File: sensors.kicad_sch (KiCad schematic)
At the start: 9 parts, among them J3 Conn_01x04, U10 MPU-9250, U12 LSM6DS3

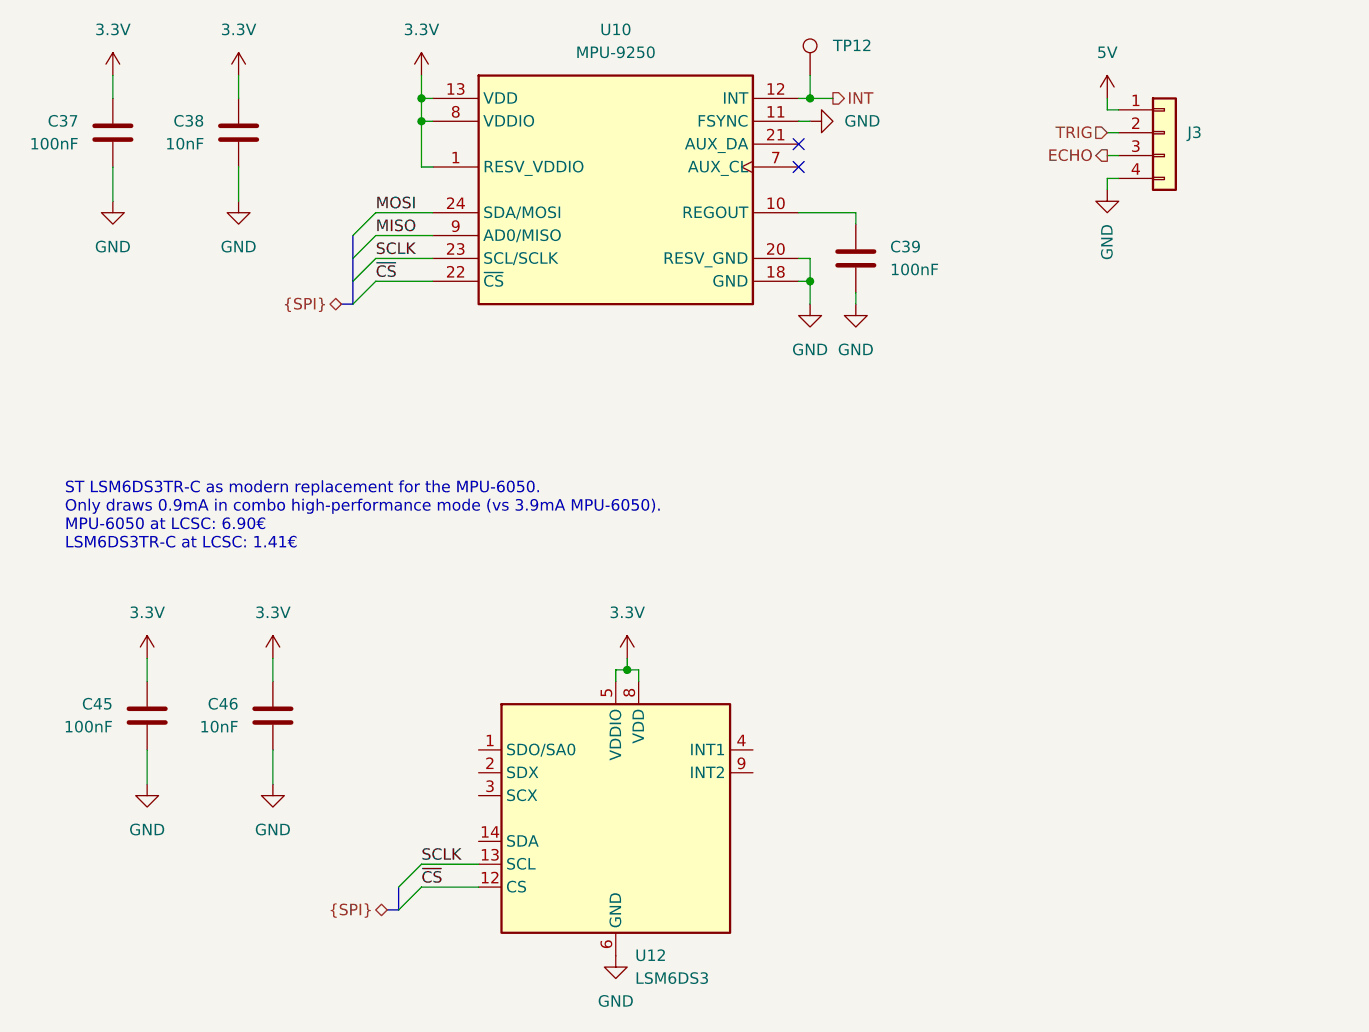
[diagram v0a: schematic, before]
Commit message: Undo component replacement
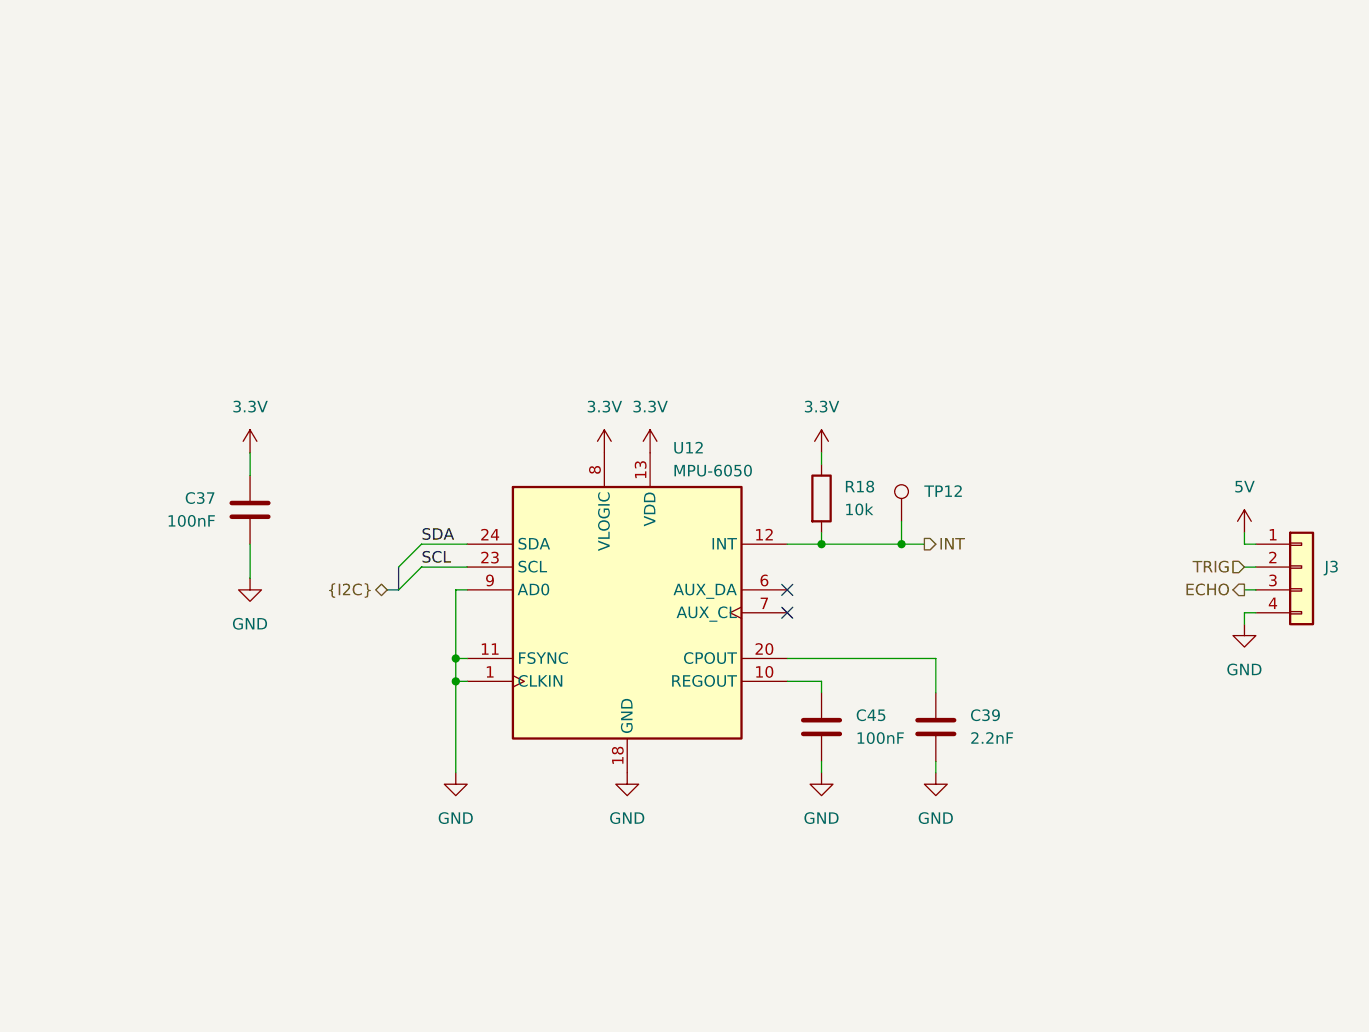
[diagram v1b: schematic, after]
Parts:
- removed C38, C46: 10nF, Capacitor_SMD:C_0402_1005Metric_Pad0.74x0.62mm_HandSolder, symbol Device:C
- removed U10: MPU-9250, Sensor_Motion:InvenSense_QFN-24_3x3mm_P0.4mm, symbol Sensor_Motion:MPU-9250
- removed U12: LSM6DS3, Package_LGA:LGA-14_3x2.5mm_P0.5mm_LayoutBorder3x4y, symbol Sensor_Motion:LSM6DS3
- added R18: 10k, symbol Device:R
- added U12: MPU-6050, Sensor_Motion:InvenSense_QFN-24_4x4mm_P0.5mm, symbol Sensor_Motion:MPU-6050
- C39: value 100nF -> 2.2nF
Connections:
- net 3.3V: now also R18.1, U12.13 (VDD), U12.8 (VLOGIC); no longer C45.1
- net GND: now also U12.1 (CLKIN), U12.11 (FSYNC), U12.18 (GND), U12.9 (AD0)
- net INT: now also R18.2, U12.12 (INT)
- net at C39.1: now also U12.20 (CPOUT)
- new net: C45.1, U12.10 (REGOUT)
- new net SCL: U12.23 (SCL)
- new net SDA: U12.24 (SDA)
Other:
- note removed: "ST LSM6DS3TR-C as modern replacement for the MPU-6050. Only draws 0.9mA in combo high-performance mode (vs 3.9mA MPU-6050). MPU-6050 at LCSC: 6.90€ LSM6DS3TR-C at LCSC: 1.41€"
- moved on the sheet: C37, C39, J3, TP12

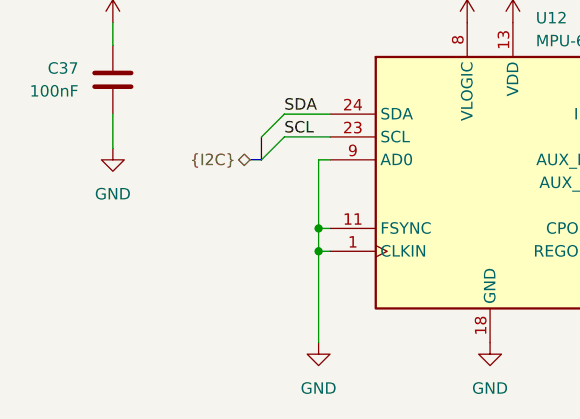
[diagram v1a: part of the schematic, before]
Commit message: Document address assignment
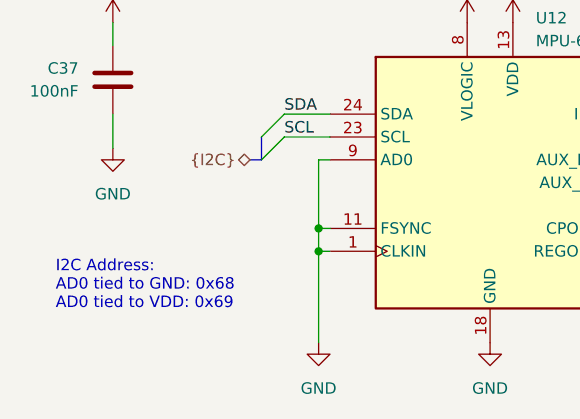
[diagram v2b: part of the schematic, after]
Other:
- note added: "I2C Address: AD0 tied to GND: 0x68 AD0 tied to VDD: 0x69"
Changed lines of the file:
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@@
 		(members "IN1" "IN2" "PWM")
+	)
+	(text "I2C Address:\nAD0 tied to GND: 0x68\nAD0 tied to VDD: 0x69"
+		(exclude_from_sim no)
+		(at 95.25 109.22 0)
+		(effects
+			(font
+				(size 1.27 1.27)
+			)
+			(justify left)
+		)
 	)
 	(junction

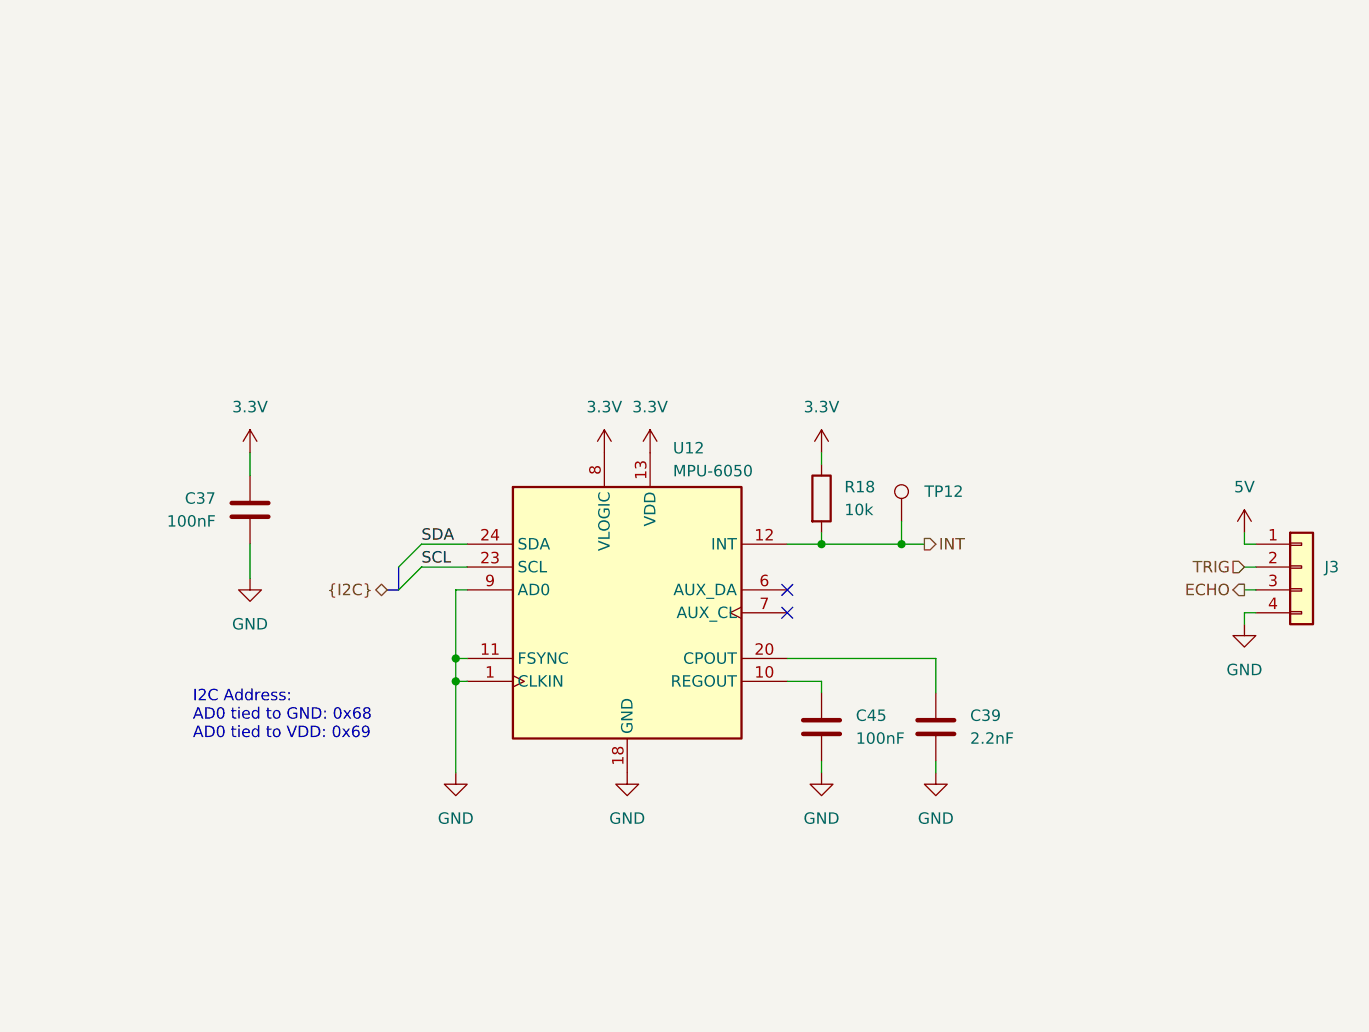
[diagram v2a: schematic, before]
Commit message: Fix sensor wiring
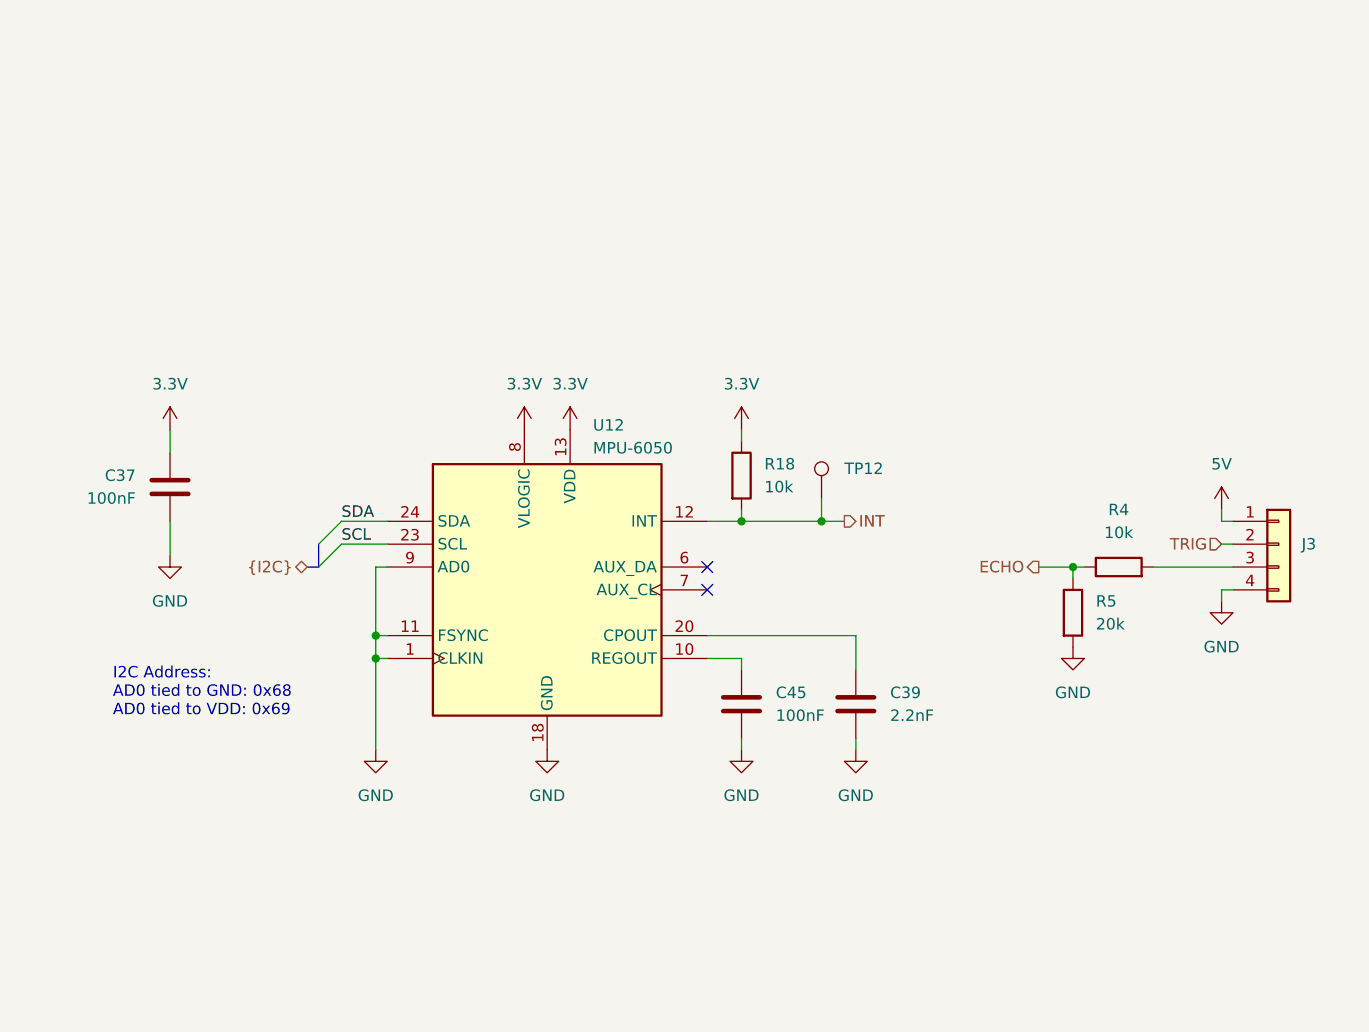
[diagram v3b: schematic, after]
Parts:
- added R4: 10k, symbol Device:R
- added R5: 20k, symbol Device:R
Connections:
- net ECHO: now also R4.1, R5.1; no longer J3.3 (Pin_3)
- net GND: now also R5.2
- new net: J3.3 (Pin_3), R4.2
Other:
- moved on the sheet: C37, C39, C45, J3, R18, TP12, U12

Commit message: Add missing pull-up for CP2102
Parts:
- renumbered C37 to C38, C45 to C39, C39 to C40, J3 to J4, R18 to R17, R4 to R18, R5 to R19, U12 to U10
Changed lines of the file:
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@@
 		(on_board yes)
 		(dnp no)
-		(property "Reference" "J3"
+		(property "Reference" "J4"
 			(at 218.44 90.1699 0)
 			(effects
@@
 			(project "Tumbler2_Redesign"
 				(path "/f3fd8d79-9d35-4c04-811e-2697a2740958/38423c09-d546-4c9c-b674-750983dc8f27"
-					(reference "J3")
+					(reference "J4")
 					(unit 1)
 				)
@@
 		(dnp no)
 		(fields_autoplaced yes)
-		(property "Reference" "#PWR0118"
+		(property "Reference" "#PWR0130"
 			(at 115.57 119.38 0)
 			(effects
@@
 			(project "Tumbler2_Redesign"
 				(path "/f3fd8d79-9d35-4c04-811e-2697a2740958/38423c09-d546-4c9c-b674-750983dc8f27"
-					(reference "#PWR0118")
+					(reference "#PWR0130")
 					(unit 1)
 				)
@@
 		(dnp no)
 		(fields_autoplaced yes)
-		(property "Reference" "#PWR0119"
+		(property "Reference" "#PWR0122"
 			(at 92.71 81.28 0)
 			(effects
@@
 			(project "Tumbler2_Redesign"
 				(path "/f3fd8d79-9d35-4c04-811e-2697a2740958/38423c09-d546-4c9c-b674-750983dc8f27"
-					(reference "#PWR0119")
+					(reference "#PWR0122")
 					(unit 1)
 				)
@@
 		(dnp no)
 		(fields_autoplaced yes)
-		(property "Reference" "#PWR0125"
+		(property "Reference" "#PWR0127"
 			(at 92.71 97.79 0)
 			(effects
@@
 			(project "Tumbler2_Redesign"
 				(path "/f3fd8d79-9d35-4c04-811e-2697a2740958/38423c09-d546-4c9c-b674-750983dc8f27"
-					(reference "#PWR0125")
+					(reference "#PWR0127")
 					(unit 1)
 				)
@@
 		(dnp no)
 		(fields_autoplaced yes)
-		(property "Reference" "R5"
+		(property "Reference" "R19"
 			(at 195.58 96.5199 0)
 			(effects
@@
 			(project "Tumbler2_Redesign"
 				(path "/f3fd8d79-9d35-4c04-811e-2697a2740958/38423c09-d546-4c9c-b674-750983dc8f27"
-					(reference "R5")
+					(reference "R19")
 					(unit 1)
 				)
@@
 		(dnp no)
 		(fields_autoplaced yes)
-		(property "Reference" "R18"
+		(property "Reference" "R17"
 			(at 158.75 81.2799 0)
 			(effects
@@
 			(project "Tumbler2_Redesign"
 				(path "/f3fd8d79-9d35-4c04-811e-2697a2740958/38423c09-d546-4c9c-b674-750983dc8f27"
-					(reference "R18")
+					(reference "R17")
 					(unit 1)
 				)
@@
 		(dnp no)
 		(fields_autoplaced yes)
-		(property "Reference" "#PWR0122"
+		(property "Reference" "#PWR0131"
 			(at 134.62 119.38 0)
 			(effects
@@
 			(project "Tumbler2_Redesign"
 				(path "/f3fd8d79-9d35-4c04-811e-2697a2740958/38423c09-d546-4c9c-b674-750983dc8f27"
-					(reference "#PWR0122")
+					(reference "#PWR0131")
 					(unit 1)
 				)
@@
 		(on_board yes)
 		(dnp no)
-		(property "Reference" "R4"
+		(property "Reference" "R18"
 			(at 198.12 86.36 90)
 			(effects
@@
 			(project "Tumbler2_Redesign"
 				(path "/f3fd8d79-9d35-4c04-811e-2697a2740958/38423c09-d546-4c9c-b674-750983dc8f27"
-					(reference "R4")
+					(reference "R18")
 					(unit 1)
 				)
@@
 		(dnp no)
 		(fields_autoplaced yes)
-		(property "Reference" "C39"
+		(property "Reference" "C40"
 			(at 172.72 106.6799 0)
 			(effects
@@
 			(project "Tumbler2_Redesign"
 				(path "/f3fd8d79-9d35-4c04-811e-2697a2740958/38423c09-d546-4c9c-b674-750983dc8f27"
-					(reference "C39")
+					(reference "C40")
 					(unit 1)
 				)
@@
 		(dnp no)
 		(fields_autoplaced yes)
-		(property "Reference" "#PWR0120"
+		(property "Reference" "#PWR0124"
 			(at 137.16 81.28 0)
 			(effects
@@
 			(project "Tumbler2_Redesign"
 				(path "/f3fd8d79-9d35-4c04-811e-2697a2740958/38423c09-d546-4c9c-b674-750983dc8f27"
-					(reference "#PWR0120")
+					(reference "#PWR0124")
 					(unit 1)
 				)
@@
 		(dnp no)
 		(fields_autoplaced yes)
-		(property "Reference" "#PWR0127"
+		(property "Reference" "#PWR0133"
 			(at 168.91 119.38 0)
 			(effects
@@
 			(project "Tumbler2_Redesign"
 				(path "/f3fd8d79-9d35-4c04-811e-2697a2740958/38423c09-d546-4c9c-b674-750983dc8f27"
-					(reference "#PWR0127")
+					(reference "#PWR0133")
 					(unit 1)
 				)
@@
 		(on_board yes)
 		(dnp no)
-		(property "Reference" "U12"
+		(property "Reference" "U10"
 			(at 139.7 76.962 0)
 			(effects
@@
 			(project ""
 				(path "/f3fd8d79-9d35-4c04-811e-2697a2740958/38423c09-d546-4c9c-b674-750983dc8f27"
-					(reference "U12")
+					(reference "U10")
 					(unit 1)
 				)
@@
 		(dnp no)
 		(fields_autoplaced yes)
-		(property "Reference" "#PWR0124"
+		(property "Reference" "#PWR0125"
 			(at 156.21 81.28 0)
 			(effects
@@
 			(project "Tumbler2_Redesign"
 				(path "/f3fd8d79-9d35-4c04-811e-2697a2740958/38423c09-d546-4c9c-b674-750983dc8f27"
-					(reference "#PWR0124")
+					(reference "#PWR0125")
 					(unit 1)
 				)
@@
 		(dnp no)
 		(fields_autoplaced yes)
-		(property "Reference" "#PWR053"
+		(property "Reference" "#PWR0129"
 			(at 193.04 107.95 0)
 			(effects
@@
 			(project "Tumbler2_Redesign"
 				(path "/f3fd8d79-9d35-4c04-811e-2697a2740958/38423c09-d546-4c9c-b674-750983dc8f27"
-					(reference "#PWR053")
+					(reference "#PWR0129")
 					(unit 1)
 				)
@@
 		(dnp no)
 		(fields_autoplaced yes)
-		(property "Reference" "#PWR0126"
+		(property "Reference" "#PWR0132"
 			(at 156.21 119.38 0)
 			(effects
@@
 			(project "Tumbler2_Redesign"
 				(path "/f3fd8d79-9d35-4c04-811e-2697a2740958/38423c09-d546-4c9c-b674-750983dc8f27"
-					(reference "#PWR0126")
+					(reference "#PWR0132")
 					(unit 1)
 				)
@@
 		(dnp no)
 		(fields_autoplaced yes)
-		(property "Reference" "#PWR0146"
+		(property "Reference" "#PWR0128"
 			(at 209.55 102.87 0)
 			(effects
@@
 			(project "Tumbler2_Redesign"
 				(path "/f3fd8d79-9d35-4c04-811e-2697a2740958/38423c09-d546-4c9c-b674-750983dc8f27"
-					(reference "#PWR0146")
+					(reference "#PWR0128")
 					(unit 1)
 				)
@@
 		(dnp no)
 		(fields_autoplaced yes)
-		(property "Reference" "C45"
+		(property "Reference" "C39"
 			(at 160.02 106.6799 0)
 			(effects
@@
 			(project "Tumbler2_Redesign"
 				(path "/f3fd8d79-9d35-4c04-811e-2697a2740958/38423c09-d546-4c9c-b674-750983dc8f27"
-					(reference "C45")
+					(reference "C39")
 					(unit 1)
 				)
@@
 		(dnp no)
 		(fields_autoplaced yes)
-		(property "Reference" "#PWR0121"
+		(property "Reference" "#PWR0126"
 			(at 209.55 90.17 0)
 			(effects
@@
 			(project "Tumbler2_Redesign"
 				(path "/f3fd8d79-9d35-4c04-811e-2697a2740958/38423c09-d546-4c9c-b674-750983dc8f27"
-					(reference "#PWR0121")
+					(reference "#PWR0126")
 					(unit 1)
 				)
@@
 		(on_board yes)
 		(dnp no)
-		(property "Reference" "C37"
+		(property "Reference" "C38"
 			(at 88.9 82.5499 0)
 			(effects
@@
 			(project "Tumbler2_Redesign"
 				(path "/f3fd8d79-9d35-4c04-811e-2697a2740958/38423c09-d546-4c9c-b674-750983dc8f27"
-					(reference "C37")
-					(unit 1)
-				)
+					(reference "C38")
+					(unit 1)
+				)
